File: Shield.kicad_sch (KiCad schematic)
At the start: 9 parts, among them U1 MIC5219-3.3YM5, U2 MIC5219-3.3YM5

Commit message: 0 DRC
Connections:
- no-connect marks 0 -> 20
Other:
- sheet MAX31865_1 ports: added none; removed DRDY
- sheet MAX31865_2 ports: added none; removed DRDY
- sheet MAX31865_3 ports: added none; removed DRDY
- sheet MAX31865_4 ports: added none; removed DRDY
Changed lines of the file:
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@@
   (junction (at 82.55 72.39) (diameter 0) (color 0 0 0 0)
   )
+  (no_connect (at 177.8 52.07))
+  (no_connect (at 162.56 36.83))
+  (no_connect (at 167.64 36.83))
+  (no_connect (at 152.4 64.77))
+  (no_connect (at 152.4 54.61))
+  (no_connect (at 152.4 72.39))
+  (no_connect (at 177.8 57.15))
+  (no_connect (at 177.8 80.01))
+  (no_connect (at 152.4 52.07))
+  (no_connect (at 177.8 74.93))
+  (no_connect (at 177.8 82.55))
+  (no_connect (at 152.4 62.23))
+  (no_connect (at 177.8 46.99))
+  (no_connect (at 152.4 49.53))
+  (no_connect (at 152.4 59.69))
+  (no_connect (at 152.4 46.99))
+  (no_connect (at 152.4 57.15))
+  (no_connect (at 177.8 72.39))
+  (no_connect (at 152.4 69.85))
+  (no_connect (at 152.4 67.31))
   (wire (pts (xy 82.55 44.45) (xy 82.55 52.07))
     (stroke (width 0) (type default) (color 0 0 0 0))
@@
     (stroke (width 0) (type default) (color 0 0 0 0))
   )
+  (wire (pts (xy 172.72 96.52) (xy 165.1 96.52))
+    (stroke (width 0) (type default) (color 0 0 0 0))
+  )
   (wire (pts (xy 233.68 92.71) (xy 241.3 92.71))
     (stroke (width 0) (type default) (color 0 0 0 0))
@@
     (stroke (width 0) (type default) (color 0 0 0 0))
   )
+  (wire (pts (xy 170.18 33.02) (xy 170.18 36.83))
+    (stroke (width 0) (type default) (color 0 0 0 0))
+  )
   (wire (pts (xy 233.68 49.53) (xy 241.3 49.53))
     (stroke (width 0) (type default) (color 0 0 0 0))
@@
     (stroke (width 0) (type default) (color 0 0 0 0))
   )
-  (wire (pts (xy 170.18 33.02) (xy 170.18 36.83))
-    (stroke (width 0) (type default) (color 0 0 0 0))
-  )
   (wire (pts (xy 31.75 72.39) (xy 31.75 78.74))
     (stroke (width 0) (type default) (color 0 0 0 0))
   )
+  (wire (pts (xy 52.07 82.55) (xy 52.07 93.98))
+    (stroke (width 0) (type default) (color 0 0 0 0))
+  )
   (wire (pts (xy 24.13 31.75) (xy 31.75 31.75))
     (stroke (width 0) (type default) (color 0 0 0 0))
@@
     (stroke (width 0) (type default) (color 0 0 0 0))
   )
-  (wire (pts (xy 52.07 82.55) (xy 52.07 93.98))
-    (stroke (width 0) (type default) (color 0 0 0 0))
-  )
   (wire (pts (xy 39.37 31.75) (xy 39.37 34.29))
+    (stroke (width 0) (type default) (color 0 0 0 0))
+  )
+  (wire (pts (xy 172.72 97.79) (xy 172.72 96.52))
     (stroke (width 0) (type default) (color 0 0 0 0))
   )
@@
     )
     (property "Datasheet" "" (id 3) (at 52.07 53.34 0)
+      (effects (font (size 1.27 1.27)) hide)
+    )
+    (pin "1")
+  )
+  (symbol (lib_id "power:PWR_FLAG") (at 172.72 97.79 180) (unit 1)
+    (in_bom yes) (on_board yes) (fields_autoplaced)
+    (property "Reference" "#FLG0102" (id 0) (at 172.72 99.695 0)
+      (effects (font (size 1.27 1.27)) hide)
+    )
+    (property "Value" "PWR_FLAG" (id 1) (at 172.72 102.87 0))
+    (property "Footprint" "" (id 2) (at 172.72 97.79 0)
+      (effects (font (size 1.27 1.27)) hide)
+    )
+    (property "Datasheet" "~" (id 3) (at 172.72 97.79 0)
       (effects (font (size 1.27 1.27)) hide)
     )
@@
       (effects (font (size 1.27 1.27)) (justify left))
     )
-    (pin "DRDY" output (at 241.3 85.09 180)
-      (effects (font (size 1.27 1.27)) (justify left))
-    )
   )
   (sheet (at 241.3 62.23) (size 29.21 15.24) (fields_autoplaced)
@@
       (effects (font (size 1.27 1.27)) (justify left))
     )
-    (pin "DRDY" output (at 241.3 63.5 180)
-      (effects (font (size 1.27 1.27)) (justify left))
-    )
   )
   (sheet (at 241.3 40.64) (size 29.21 15.24) (fields_autoplaced)
@@
       (effects (font (size 1.27 1.27)) (justify left))
     )
-    (pin "DRDY" output (at 241.3 41.91 180)
-      (effects (font (size 1.27 1.27)) (justify left))
-    )
   )
   (sheet (at 241.3 17.78) (size 29.21 15.24) (fields_autoplaced)
@@
     )
     (pin "CS" input (at 241.3 29.21 180)
-      (effects (font (size 1.27 1.27)) (justify left))
-    )
-    (pin "DRDY" output (at 241.3 19.05 180)
       (effects (font (size 1.27 1.27)) (justify left))
     )
@@
   )
   (symbol_instances
+    (path "/9b89f10a-1c70-4b37-9e6c-a2d5f4afe714"
+      (reference "#FLG0102") (unit 1) (value "PWR_FLAG") (footprint "")
+    )
     (path "/65894402-c226-402d-b5d6-04dda99e0b28"
       (reference "#PWR01") (unit 1) (value "+5V") (footprint "")

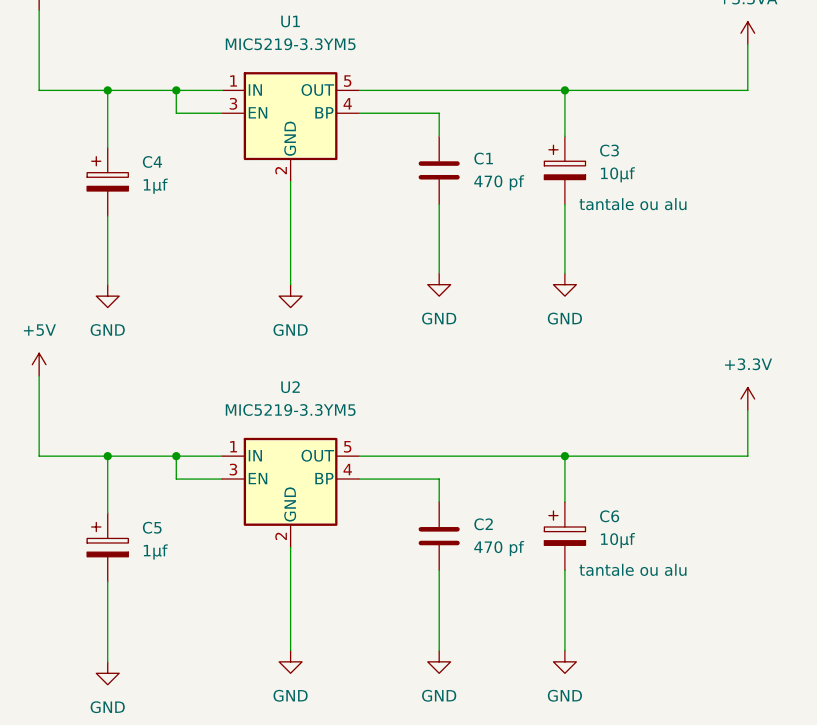
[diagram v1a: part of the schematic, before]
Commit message: Passe l'empreinte en TSOP
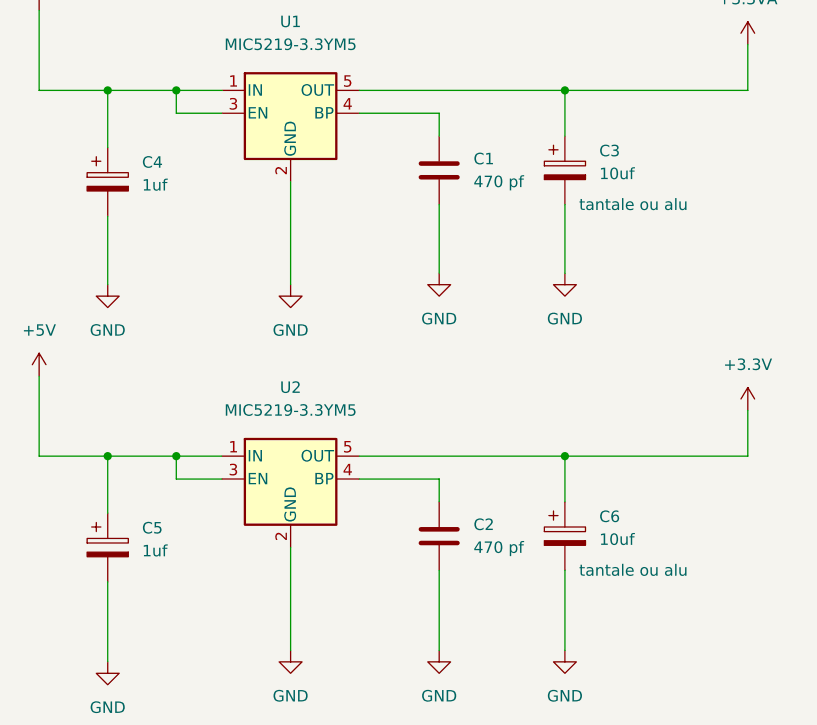
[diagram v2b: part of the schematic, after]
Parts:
- C3, C6: value 10µf -> 10uf; footprint Capacitor_Tantalum_SMD:CP_EIA-3216-18_Kemet-A_Pad1.58x1.35mm_HandSolder -> Capacitor_Tantalum_SMD:CP_EIA-3216-18_Kemet-A
- C4, C5: value 1µf -> 1uf; footprint Capacitor_Tantalum_SMD:CP_EIA-3216-18_Kemet-A_Pad1.58x1.35mm_HandSolder -> Capacitor_Tantalum_SMD:CP_EIA-3216-18_Kemet-A
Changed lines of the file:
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@@
       (effects (font (size 1.27 1.27)) (justify left))
     )
-    (property "Value" "10µf " (id 1) (at 86.36 41.0209 0)
-      (effects (font (size 1.27 1.27)) (justify left))
-    )
-    (property "Footprint" "Capacitor_Tantalum_SMD:CP_EIA-3216-18_Kemet-A_Pad1.58x1.35mm_HandSolder" (id 2) (at 83.5152 44.45 0)
+    (property "Value" "10uf " (id 1) (at 86.36 41.0209 0)
+      (effects (font (size 1.27 1.27)) (justify left))
+    )
+    (property "Footprint" "Capacitor_Tantalum_SMD:CP_EIA-3216-18_Kemet-A" (id 2) (at 83.5152 44.45 0)
       (effects (font (size 1.27 1.27)) hide)
     )
@@
       (effects (font (size 1.27 1.27)) (justify left))
     )
-    (property "Value" "1µf " (id 1) (at 35.56 42.2909 0)
-      (effects (font (size 1.27 1.27)) (justify left))
-    )
-    (property "Footprint" "Capacitor_Tantalum_SMD:CP_EIA-3216-18_Kemet-A_Pad1.58x1.35mm_HandSolder" (id 2) (at 32.7152 45.72 0)
+    (property "Value" "1uf " (id 1) (at 35.56 42.2909 0)
+      (effects (font (size 1.27 1.27)) (justify left))
+    )
+    (property "Footprint" "Capacitor_Tantalum_SMD:CP_EIA-3216-18_Kemet-A" (id 2) (at 32.7152 45.72 0)
       (effects (font (size 1.27 1.27)) hide)
     )
@@
       (effects (font (size 1.27 1.27)) (justify left))
     )
-    (property "Value" "10µf " (id 1) (at 86.36 81.6609 0)
-      (effects (font (size 1.27 1.27)) (justify left))
-    )
-    (property "Footprint" "Capacitor_Tantalum_SMD:CP_EIA-3216-18_Kemet-A_Pad1.58x1.35mm_HandSolder" (id 2) (at 83.5152 85.09 0)
+    (property "Value" "10uf " (id 1) (at 86.36 81.6609 0)
+      (effects (font (size 1.27 1.27)) (justify left))
+    )
+    (property "Footprint" "Capacitor_Tantalum_SMD:CP_EIA-3216-18_Kemet-A" (id 2) (at 83.5152 85.09 0)
       (effects (font (size 1.27 1.27)) hide)
     )
@@
       (effects (font (size 1.27 1.27)) (justify left))
     )
-    (property "Value" "1µf " (id 1) (at 35.56 82.9309 0)
-      (effects (font (size 1.27 1.27)) (justify left))
-    )
-    (property "Footprint" "Capacitor_Tantalum_SMD:CP_EIA-3216-18_Kemet-A_Pad1.58x1.35mm_HandSolder" (id 2) (at 32.7152 86.36 0)
+    (property "Value" "1uf " (id 1) (at 35.56 82.9309 0)
+      (effects (font (size 1.27 1.27)) (justify left))
+    )
+    (property "Footprint" "Capacitor_Tantalum_SMD:CP_EIA-3216-18_Kemet-A" (id 2) (at 32.7152 86.36 0)
       (effects (font (size 1.27 1.27)) hide)
     )
@@
     )
     (path "/b0f180b9-4197-4edd-b5e1-238f1d62e083"
-      (reference "C3") (unit 1) (value "10µf ") (footprint "Capacitor_Tantalum_SMD:CP_EIA-3216-18_Kemet-A_Pad1.58x1.35mm_HandSolder")
+      (reference "C3") (unit 1) (value "10uf ") (footprint "Capacitor_Tantalum_SMD:CP_EIA-3216-18_Kemet-A")
     )
     (path "/c2d4c3d3-978a-4b0e-9031-6b694cad1a9a"
-      (reference "C4") (unit 1) (value "1µf ") (footprint "Capacitor_Tantalum_SMD:CP_EIA-3216-18_Kemet-A_Pad1.58x1.35mm_HandSolder")
+      (reference "C4") (unit 1) (value "1uf ") (footprint "Capacitor_Tantalum_SMD:CP_EIA-3216-18_Kemet-A")
     )
     (path "/fcf8fc47-e029-49c8-9cbf-c4c4f1034b3f"
-      (reference "C5") (unit 1) (value "1µf ") (footprint "Capacitor_Tantalum_SMD:CP_EIA-3216-18_Kemet-A_Pad1.58x1.35mm_HandSolder")
+      (reference "C5") (unit 1) (value "1uf ") (footprint "Capacitor_Tantalum_SMD:CP_EIA-3216-18_Kemet-A")
     )
     (path "/f4f53a79-95c2-48d7-b683-9d56ba11ad99"
-      (reference "C6") (unit 1) (value "10µf ") (footprint "Capacitor_Tantalum_SMD:CP_EIA-3216-18_Kemet-A_Pad1.58x1.35mm_HandSolder")
+      (reference "C6") (unit 1) (value "10uf ") (footprint "Capacitor_Tantalum_SMD:CP_EIA-3216-18_Kemet-A")
     )
     (path "/ec1f69e3-5897-4f77-9f27-39305d91428f/11365b72-7dfc-4463-9cbd-3a437b9b5ec6"
@@
       (reference "U2") (unit 1) (value "MIC5219-3.3YM5") (footprint "Package_TO_SOT_SMD:SOT-23-5")
     )
+    (path "/cecccb11-9ba5-4726-b914-0eb04ce5992d/0f7ebff1-b6a9-4a4c-9024-61e0cb0cec58"
+      (reference "U?") (unit 1) (value "MAX31865xTP") (footprint "Package_DFN_QFN:TQFN-20-1EP_5x5mm_P0.65mm_EP3.25x3.25mm")
+    )
+    (path "/e2d18e8c-1174-4a60-a6fc-991b63e21af0/0f7ebff1-b6a9-4a4c-9024-61e0cb0cec58"
+      (reference "U?") (unit 1) (value "MAX31865xTP") (footprint "Package_DFN_QFN:TQFN-20-1EP_5x5mm_P0.65mm_EP3.25x3.25mm")
+    )
     (path "/ec1f69e3-5897-4f77-9f27-39305d91428f/0f7ebff1-b6a9-4a4c-9024-61e0cb0cec58"
-      (reference "U3") (unit 1) (value "MAX31865xAP") (footprint "Package_SO:SSOP-20_5.3x7.2mm_P0.65mm")
-    )
-    (path "/e2d18e8c-1174-4a60-a6fc-991b63e21af0/0f7ebff1-b6a9-4a4c-9024-61e0cb0cec58"
-      (reference "U4") (unit 1) (value "MAX31865xAP") (footprint "Package_SO:SSOP-20_5.3x7.2mm_P0.65mm")
-    )
-    (path "/cecccb11-9ba5-4726-b914-0eb04ce5992d/0f7ebff1-b6a9-4a4c-9024-61e0cb0cec58"
-      (reference "U5") (unit 1) (value "MAX31865xAP") (footprint "Package_SO:SSOP-20_5.3x7.2mm_P0.65mm")
+      (reference "U?") (unit 1) (value "MAX31865xTP") (footprint "Package_DFN_QFN:TQFN-20-1EP_5x5mm_P0.65mm_EP3.25x3.25mm")
     )
     (path "/7a39c683-02c0-4bd5-8c0c-94c88f5499d8/0f7ebff1-b6a9-4a4c-9024-61e0cb0cec58"
-      (reference "U6") (unit 1) (value "MAX31865xAP") (footprint "Package_SO:SSOP-20_5.3x7.2mm_P0.65mm")
-    )
-  )
+      (reference "U?") (unit 1) (value "MAX31865xTP") (footprint "Package_DFN_QFN:TQFN-20-1EP_5x5mm_P0.65mm_EP3.25x3.25mm")
+    )
+  )

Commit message: Passe certaine empreinte en 0603
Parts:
- C1, C2: footprint Capacitor_SMD:C_0805_2012Metric_Pad1.18x1.45mm_HandSolder -> Capacitor_SMD:C_0603_1608Metric_Pad1.08x0.95mm_HandSolder
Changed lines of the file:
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@@
       (effects (font (size 1.27 1.27)) (justify left))
     )
-    (property "Footprint" "Capacitor_SMD:C_0805_2012Metric_Pad1.18x1.45mm_HandSolder" (id 2) (at 69.5452 85.09 0)
+    (property "Footprint" "Capacitor_SMD:C_0603_1608Metric_Pad1.08x0.95mm_HandSolder" (id 2) (at 69.5452 85.09 0)
       (effects (font (size 1.27 1.27)) hide)
     )
@@
       (effects (font (size 1.27 1.27)) (justify left))
     )
-    (property "Footprint" "Capacitor_SMD:C_0805_2012Metric_Pad1.18x1.45mm_HandSolder" (id 2) (at 69.5452 44.45 0)
+    (property "Footprint" "Capacitor_SMD:C_0603_1608Metric_Pad1.08x0.95mm_HandSolder" (id 2) (at 69.5452 44.45 0)
       (effects (font (size 1.27 1.27)) hide)
     )
@@
     )
     (path "/c49d794b-82e9-493d-b715-0ad5480931c3"
-      (reference "C1") (unit 1) (value "470 pf") (footprint "Capacitor_SMD:C_0805_2012Metric_Pad1.18x1.45mm_HandSolder")
+      (reference "C1") (unit 1) (value "470 pf") (footprint "Capacitor_SMD:C_0603_1608Metric_Pad1.08x0.95mm_HandSolder")
     )
     (path "/86a05c3c-54d2-4977-bcb6-ee4c0872ef57"
-      (reference "C2") (unit 1) (value "470 pf") (footprint "Capacitor_SMD:C_0805_2012Metric_Pad1.18x1.45mm_HandSolder")
+      (reference "C2") (unit 1) (value "470 pf") (footprint "Capacitor_SMD:C_0603_1608Metric_Pad1.08x0.95mm_HandSolder")
     )
     (path "/b0f180b9-4197-4edd-b5e1-238f1d62e083"
@@
     )
     (path "/ec1f69e3-5897-4f77-9f27-39305d91428f/11365b72-7dfc-4463-9cbd-3a437b9b5ec6"
-      (reference "C7") (unit 1) (value "100nF") (footprint "Capacitor_SMD:C_0805_2012Metric_Pad1.18x1.45mm_HandSolder")
+      (reference "C7") (unit 1) (value "100nF") (footprint "Capacitor_SMD:C_0603_1608Metric_Pad1.08x0.95mm_HandSolder")
     )
     (path "/ec1f69e3-5897-4f77-9f27-39305d91428f/a20bec16-7915-439c-a056-303745291c4b"
-      (reference "C8") (unit 1) (value "100nF") (footprint "Capacitor_SMD:C_0805_2012Metric_Pad1.18x1.45mm_HandSolder")
+      (reference "C8") (unit 1) (value "100nF") (footprint "Capacitor_SMD:C_0603_1608Metric_Pad1.08x0.95mm_HandSolder")
     )
     (path "/e2d18e8c-1174-4a60-a6fc-991b63e21af0/11365b72-7dfc-4463-9cbd-3a437b9b5ec6"
-      (reference "C9") (unit 1) (value "100nF") (footprint "Capacitor_SMD:C_0805_2012Metric_Pad1.18x1.45mm_HandSolder")
+      (reference "C9") (unit 1) (value "100nF") (footprint "Capacitor_SMD:C_0603_1608Metric_Pad1.08x0.95mm_HandSolder")
     )
     (path "/ec1f69e3-5897-4f77-9f27-39305d91428f/ecb3c446-1256-4640-ae70-3636a855c193"
-      (reference "C10") (unit 1) (value "100nF") (footprint "Capacitor_SMD:C_0805_2012Metric_Pad1.18x1.45mm_HandSolder")
+      (reference "C10") (unit 1) (value "100nF") (footprint "Capacitor_SMD:C_0603_1608Metric_Pad1.08x0.95mm_HandSolder")
     )
     (path "/e2d18e8c-1174-4a60-a6fc-991b63e21af0/a20bec16-7915-439c-a056-303745291c4b"
-      (reference "C11") (unit 1) (value "100nF") (footprint "Capacitor_SMD:C_0805_2012Metric_Pad1.18x1.45mm_HandSolder")
+      (reference "C11") (unit 1) (value "100nF") (footprint "Capacitor_SMD:C_0603_1608Metric_Pad1.08x0.95mm_HandSolder")
     )
     (path "/e2d18e8c-1174-4a60-a6fc-991b63e21af0/ecb3c446-1256-4640-ae70-3636a855c193"
-      (reference "C12") (unit 1) (value "100nF") (footprint "Capacitor_SMD:C_0805_2012Metric_Pad1.18x1.45mm_HandSolder")
+      (reference "C12") (unit 1) (value "100nF") (footprint "Capacitor_SMD:C_0603_1608Metric_Pad1.08x0.95mm_HandSolder")
     )
     (path "/cecccb11-9ba5-4726-b914-0eb04ce5992d/11365b72-7dfc-4463-9cbd-3a437b9b5ec6"
-      (reference "C13") (unit 1) (value "100nF") (footprint "Capacitor_SMD:C_0805_2012Metric_Pad1.18x1.45mm_HandSolder")
+      (reference "C13") (unit 1) (value "100nF") (footprint "Capacitor_SMD:C_0603_1608Metric_Pad1.08x0.95mm_HandSolder")
     )
     (path "/cecccb11-9ba5-4726-b914-0eb04ce5992d/a20bec16-7915-439c-a056-303745291c4b"
-      (reference "C14") (unit 1) (value "100nF") (footprint "Capacitor_SMD:C_0805_2012Metric_Pad1.18x1.45mm_HandSolder")
+      (reference "C14") (unit 1) (value "100nF") (footprint "Capacitor_SMD:C_0603_1608Metric_Pad1.08x0.95mm_HandSolder")
     )
     (path "/cecccb11-9ba5-4726-b914-0eb04ce5992d/ecb3c446-1256-4640-ae70-3636a855c193"
-      (reference "C15") (unit 1) (value "100nF") (footprint "Capacitor_SMD:C_0805_2012Metric_Pad1.18x1.45mm_HandSolder")
+      (reference "C15") (unit 1) (value "100nF") (footprint "Capacitor_SMD:C_0603_1608Metric_Pad1.08x0.95mm_HandSolder")
     )
     (path "/7a39c683-02c0-4bd5-8c0c-94c88f5499d8/11365b72-7dfc-4463-9cbd-3a437b9b5ec6"
-      (reference "C16") (unit 1) (value "100nF") (footprint "Capacitor_SMD:C_0805_2012Metric_Pad1.18x1.45mm_HandSolder")
+      (reference "C16") (unit 1) (value "100nF") (footprint "Capacitor_SMD:C_0603_1608Metric_Pad1.08x0.95mm_HandSolder")
     )
     (path "/7a39c683-02c0-4bd5-8c0c-94c88f5499d8/a20bec16-7915-439c-a056-303745291c4b"
-      (reference "C17") (unit 1) (value "100nF") (footprint "Capacitor_SMD:C_0805_2012Metric_Pad1.18x1.45mm_HandSolder")
+      (reference "C17") (unit 1) (value "100nF") (footprint "Capacitor_SMD:C_0603_1608Metric_Pad1.08x0.95mm_HandSolder")
     )
     (path "/7a39c683-02c0-4bd5-8c0c-94c88f5499d8/ecb3c446-1256-4640-ae70-3636a855c193"
-      (reference "C18") (unit 1) (value "100nF") (footprint "Capacitor_SMD:C_0805_2012Metric_Pad1.18x1.45mm_HandSolder")
+      (reference "C18") (unit 1) (value "100nF") (footprint "Capacitor_SMD:C_0603_1608Metric_Pad1.08x0.95mm_HandSolder")
     )
     (path "/ec1f69e3-5897-4f77-9f27-39305d91428f/5ad22914-d2c9-4f78-8618-37e3ef89df7d"
